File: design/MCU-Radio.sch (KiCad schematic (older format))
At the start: 19 parts, among them J201 ICP, SW201 B3F-1000, SW202 B3F-1000, SW203 B3F-1000, SW204 B3F-1000, SW205 B3F-1000, U201 STM8S003F3P, U202 RDA5807M, Y201 32.768kHz

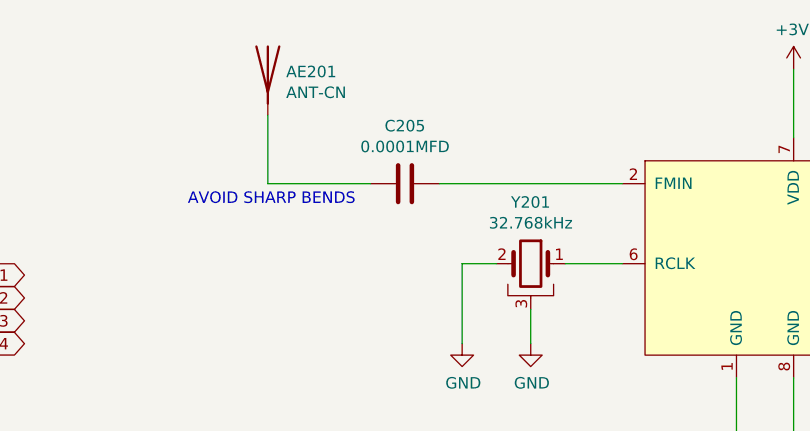
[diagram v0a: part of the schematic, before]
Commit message: Fix value of C205 capacitor. Add project ID to the readme.md file.
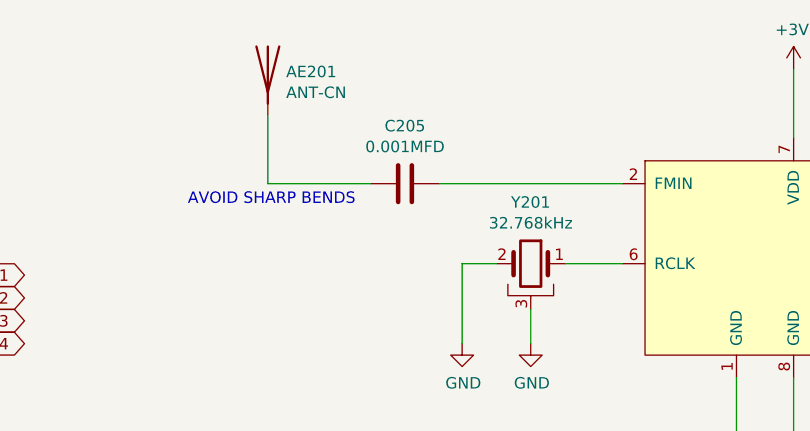
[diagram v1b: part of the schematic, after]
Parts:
- C205: value 0.0001MFD -> 0.001MFD
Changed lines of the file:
@@
 P 6700 1450
 F 0 "C205" V 6448 1450 50  0000 C CNN
-F 1 "0.0001MFD" V 6539 1450 50  0000 C CNN
+F 1 "0.001MFD" V 6539 1450 50  0000 C CNN
 F 2 "Capacitor_SMD:C_0805_2012Metric_Pad1.18x1.45mm_HandSolder" H 6738 1300 50  0001 C CNN
 F 3 "~" H 6700 1450 50  0001 C CNN
